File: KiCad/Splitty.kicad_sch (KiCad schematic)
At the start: 14 parts, among them J1 VIN (7V5 - 40VDC) 10A Max, J10 VOUT C1, J2 VOUT A1, J3 VOUT A2, J4 VOUT A3, J5 VOUT B1, J6 VOUT B2, J7 VOUT B3, J8 VOUT C3, J9 VOUT C2, SW1 10A

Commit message: Review
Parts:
- added D1: LED, symbol Device:LED
- added R1: 6K2, symbol Device:R_Small_US
- added SW2: Meter Enable, symbol Switch:SW_SPST
- U1: value ~ -> (none)
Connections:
- net at J10.1, J2.1, J3.1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: now also R1.2, SW2.2 (B); no longer U1.1 (VIN), U1.5 (VSENSE)
- net at J10.2, J2.2, J3.2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: now also D1.1 (K)
- new net: D1.2 (A), R1.1
- new net: SW2.1 (A), U1.1 (VIN), U1.5 (VSENSE)
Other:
- moved on the sheet: F1, J1, J10, J2, J3, J4, J5, J6, J7, J8, J9, SW1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

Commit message: Car Splitty
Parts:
- renumbered J7 to J10, J10 to J3, J3 to J4, J9 to J5, J4 to J6, J8 to J7, J5 to J8, J6 to J9
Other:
- added sheet Splitty Car (Splitty Car.kicad_sch)
- note added: "Red"
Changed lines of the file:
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@@
 		(company "Illusion Interactive")
 	)
-	(text "RED"
+	(text "Red"
 		(exclude_from_sim no)
-		(at 102.616 73.66 0)
+		(at 102.616 73.914 0)
 		(effects
 			(font
@@
 		(dnp no)
 		(fields_autoplaced yes)
-		(property "Reference" "J5"
+		(property "Reference" "J8"
 			(at 127 135.8899 90)
 			(show_name no)
@@
 			(project "Splitty"
 				(path "/32ee08f7-a6c8-4bf3-88d7-556af5e47718"
-					(reference "J5")
+					(reference "J8")
 					(unit 1)
 				)
@@
 		(dnp no)
 		(fields_autoplaced yes)
-		(property "Reference" "J6"
+		(property "Reference" "J9"
 			(at 146.05 135.8899 90)
 			(show_name no)
@@
 			(project "Splitty"
 				(path "/32ee08f7-a6c8-4bf3-88d7-556af5e47718"
-					(reference "J6")
+					(reference "J9")
 					(unit 1)
 				)
@@
 		(dnp no)
 		(fields_autoplaced yes)
-		(property "Reference" "J3"
+		(property "Reference" "J4"
 			(at 106.68 104.14 0)
 			(show_name no)
@@
 			(project "Splitty"
 				(path "/32ee08f7-a6c8-4bf3-88d7-556af5e47718"
-					(reference "J3")
+					(reference "J4")
 					(unit 1)
 				)
@@
 		(dnp no)
 		(fields_autoplaced yes)
-		(property "Reference" "J4"
+		(property "Reference" "J6"
 			(at 106.68 119.38 0)
 			(show_name no)
@@
 			(project "Splitty"
 				(path "/32ee08f7-a6c8-4bf3-88d7-556af5e47718"
-					(reference "J4")
+					(reference "J6")
 					(unit 1)
 				)
@@
 		(in_pos_files yes)
 		(dnp no)
-		(property "Reference" "J8"
+		(property "Reference" "J7"
 			(at 172.72 119.38 0)
 			(show_name no)
@@
 			(project "Splitty"
 				(path "/32ee08f7-a6c8-4bf3-88d7-556af5e47718"
-					(reference "J8")
+					(reference "J7")
 					(unit 1)
 				)
@@
 		(in_pos_files yes)
 		(dnp no)
-		(property "Reference" "J9"
+		(property "Reference" "J5"
 			(at 172.72 104.14 0)
 			(show_name no)
@@
 			(project "Splitty"
 				(path "/32ee08f7-a6c8-4bf3-88d7-556af5e47718"
-					(reference "J9")
+					(reference "J5")
 					(unit 1)
 				)
@@
 		(in_pos_files yes)
 		(dnp no)
-		(property "Reference" "J10"
+		(property "Reference" "J3"
 			(at 172.72 88.9 0)
 			(show_name no)
@@
 			(project "Splitty"
 				(path "/32ee08f7-a6c8-4bf3-88d7-556af5e47718"
-					(reference "J10")
+					(reference "J3")
 					(unit 1)
 				)
@@
 		(dnp no)
 		(fields_autoplaced yes)
-		(property "Reference" "J7"
+		(property "Reference" "J10"
 			(at 165.1 135.8899 90)
 			(show_name no)
@@
 			(project "Splitty"
 				(path "/32ee08f7-a6c8-4bf3-88d7-556af5e47718"
-					(reference "J7")
+					(reference "J10")
 					(unit 1)
 				)
@@
 				)
 			)
+		)
+	)
+	(sheet
+		(at 281.94 0)
+		(size 39.37 12.7)
+		(exclude_from_sim no)
+		(in_bom yes)
+		(on_board yes)
+		(dnp no)
+		(fields_autoplaced yes)
+		(stroke
+			(width 0.1524)
+			(type solid)
+		)
+		(fill
+			(color 0 0 0 0)
+		)
+		(property "Sheetname" "Splitty Car"
+			(at 281.94 -0.7116 0)
+			(show_name no)
+			(do_not_autoplace no)
+			(effects
+				(font
+					(size 1.27 1.27)
+				)
+				(justify left bottom)
+			)
+		)
+		(property "Sheetfile" "Splitty Car.kicad_sch"
+			(at 281.94 13.2846 0)
+			(show_name no)
+			(do_not_autoplace no)
+			(effects
+				(font
+					(size 1.27 1.27)
+				)
+				(justify left top)
+			)
+		)
+		(instances
+			(project "Splitty"
+				(path "/32ee08f7-a6c8-4bf3-88d7-556af5e47718"
+					(page "2")
+				)
+			)

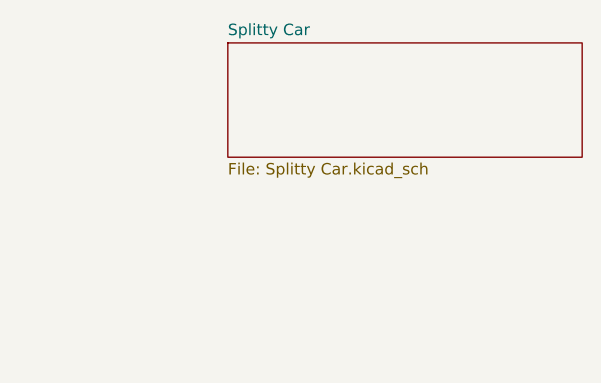
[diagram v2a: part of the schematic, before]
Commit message: Separate projects
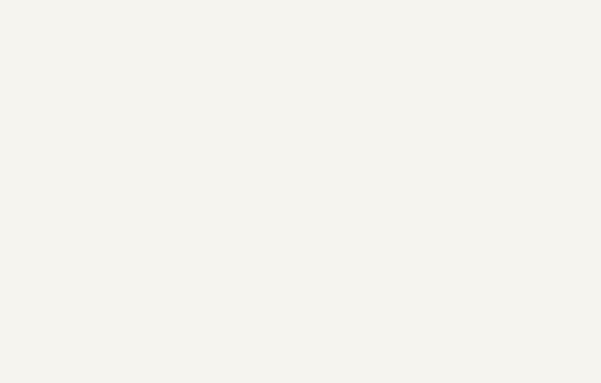
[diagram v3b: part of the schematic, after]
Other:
- removed sheet Splitty Car
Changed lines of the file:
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@@
-		)
-	)
-	(sheet
-		(at 281.94 0)
-		(size 39.37 12.7)
-		(exclude_from_sim no)
-		(in_bom yes)
-		(on_board yes)
-		(dnp no)
-		(fields_autoplaced yes)
-		(stroke
-			(width 0.1524)
-			(type solid)
-		)
-		(fill
-			(color 0 0 0 0)
-		)
-		(property "Sheetname" "Splitty Car"
-			(at 281.94 -0.7116 0)
-			(show_name no)
-			(do_not_autoplace no)
-			(effects
-				(font
-					(size 1.27 1.27)
-				)
-				(justify left bottom)
-			)
-		)
-		(property "Sheetfile" "Splitty Car.kicad_sch"
-			(at 281.94 13.2846 0)
-			(show_name no)
-			(do_not_autoplace no)
-			(effects
-				(font
-					(size 1.27 1.27)
-				)
-				(justify left top)
-			)
-		)
-		(instances
-			(project "Splitty"
-				(path "/32ee08f7-a6c8-4bf3-88d7-556af5e47718"
-					(page "2")
-				)
-			)
 		)
 	)
